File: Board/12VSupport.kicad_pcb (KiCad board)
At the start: 2 copper layers, 106.7 x 123.2 mm, 84 parts, among them J1 12V, J2 BATT, J3 BUCK_IN, J4 BUCK_OUT, J5 BOOST_IN, J6 BOOST_OUT, J7 TMP36GZ, J8 HEATER, J9 ICSP, K1 SLA-05VDC-SL-C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

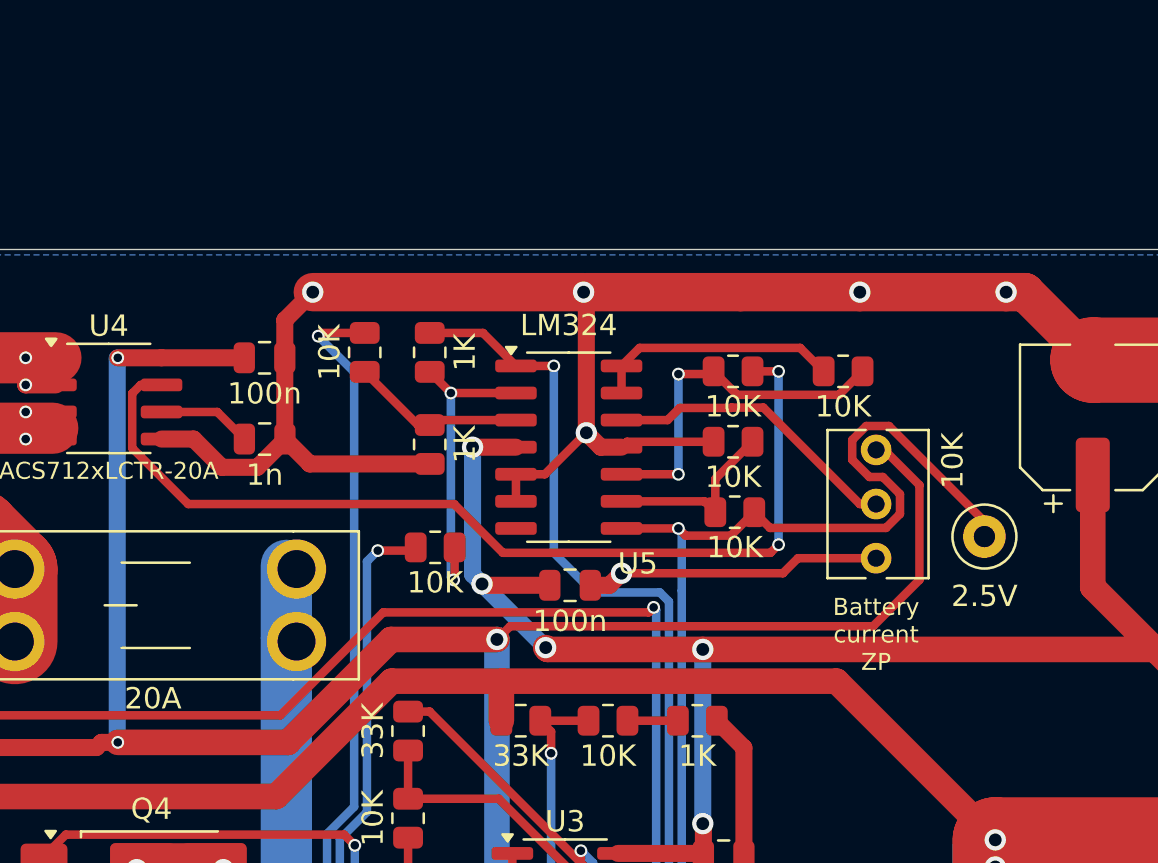
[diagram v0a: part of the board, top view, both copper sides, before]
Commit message: Schematic fixes
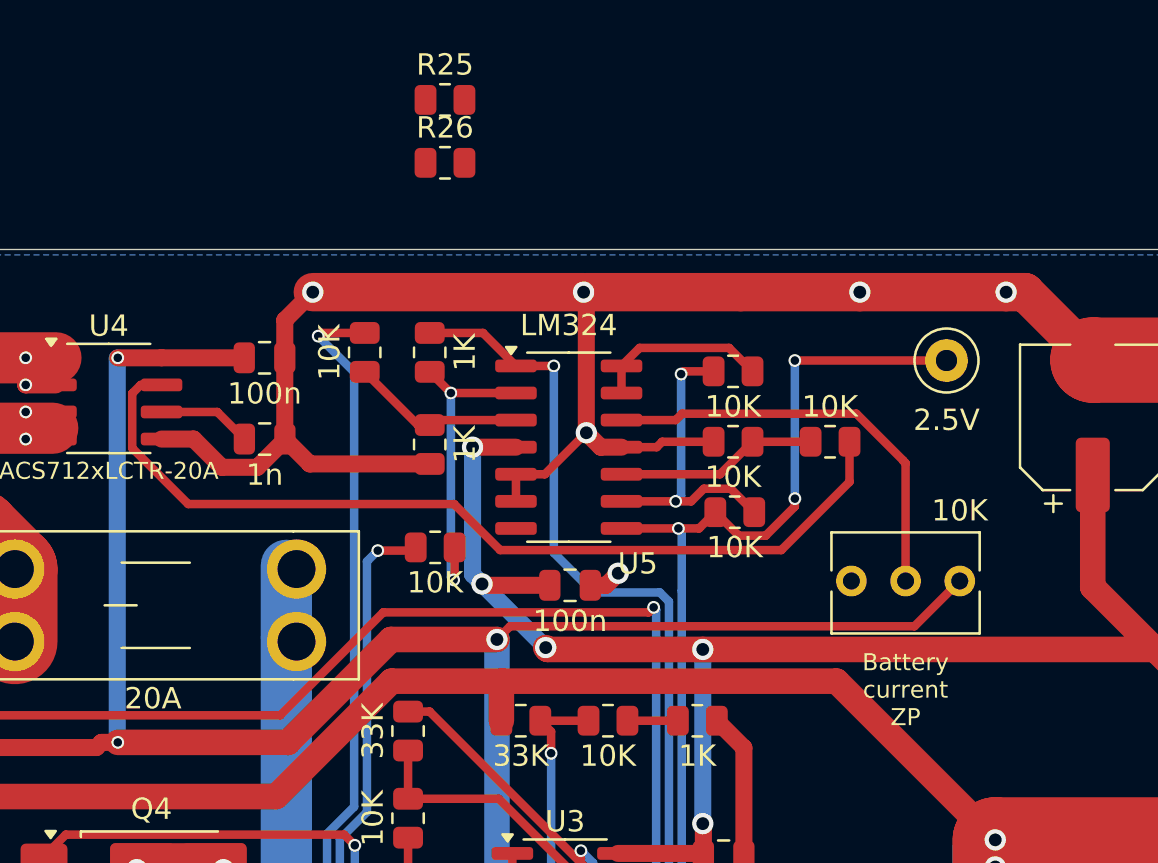
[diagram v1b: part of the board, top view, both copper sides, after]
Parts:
- added R25: 100K, Resistor_SMD:R_0805_2012Metric, F.Cu at (80.4, 34.9)
- added R26: 100K, Resistor_SMD:R_0805_2012Metric, F.Cu at (80.4, 37.8)
- moved TP1 8.44 mm to (103.9, 47.1)
- moved RV1 7.29 mm to (104.5, 57.5), turned to 0 degrees
- moved R22 3.36 mm to (98.4, 50.9), turned to 180 degrees
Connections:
- R19 pad 1: Net-(U5C--) -> CURR_SENSE
- R19 pad 2: CURR_SENSE -> Net-(U5C--)
- R20 pad 2: Net-(U5C--) -> Net-(U5C-+)
- R21 pad 1: Net-(U5C-+) -> Net-(U5C--)
- R21 pad 2: BAT_CURR -> /Sensors/VCC/2
- R22 pad 1: /Sensors/VCC/2 -> BAT_CURR
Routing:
- net GND: track 585.1 -> 572.8 mm
- net Net-(U5C-+): track 17.0 -> 9.50 mm, vias 2 -> 0
- net Net-(U5C--): track 8.63 -> 14.6 mm, vias 0 -> 2
- net Net-(U5D-+): track 14.1 -> 19.9 mm
- net VCC: track 345.4 -> 340.1 mm
- net CURR_SENSE: track 140.3 -> 135.7 mm, vias 2 -> 4
- net /Sensors/VCC/2: track 11.6 -> 7.62 mm
- net BAT_CURR: track 46.0 -> 42.9 mm, vias 2 -> 0

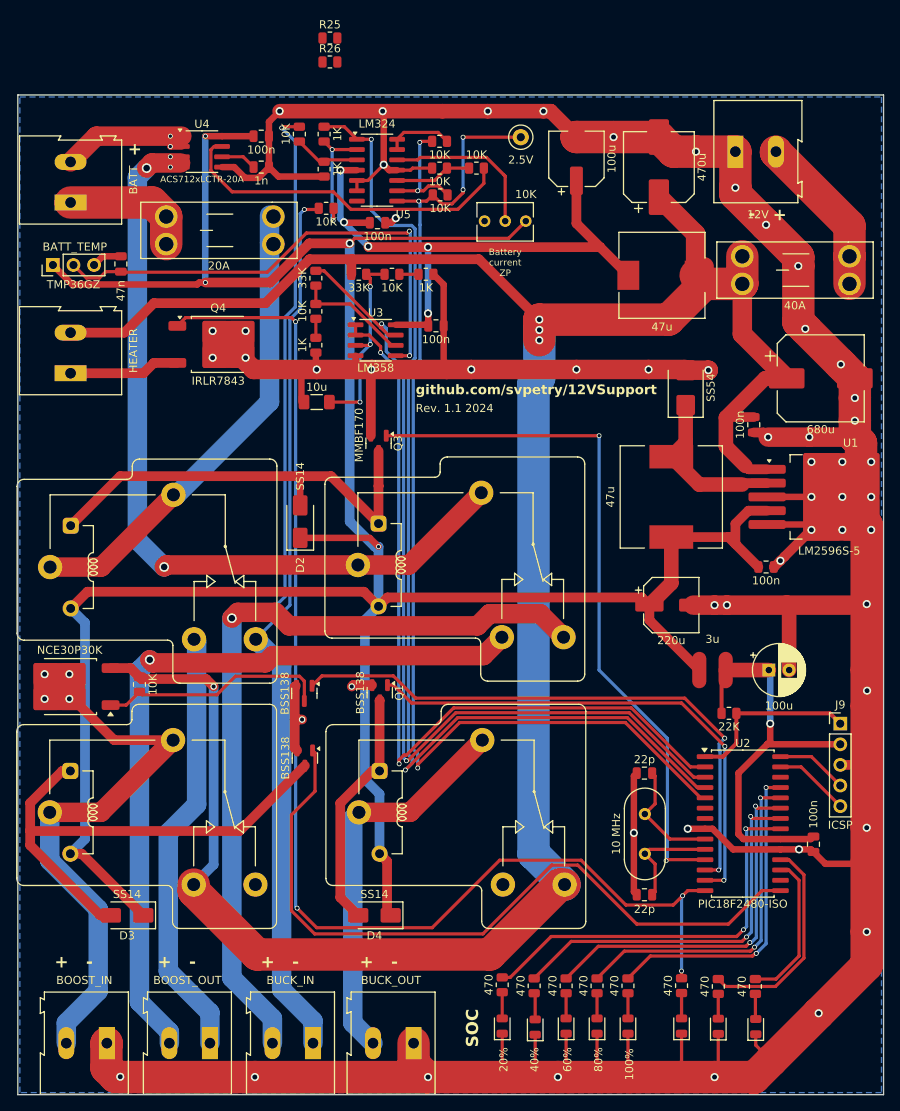
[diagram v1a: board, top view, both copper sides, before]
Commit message: Fixes battery voltage sensing.
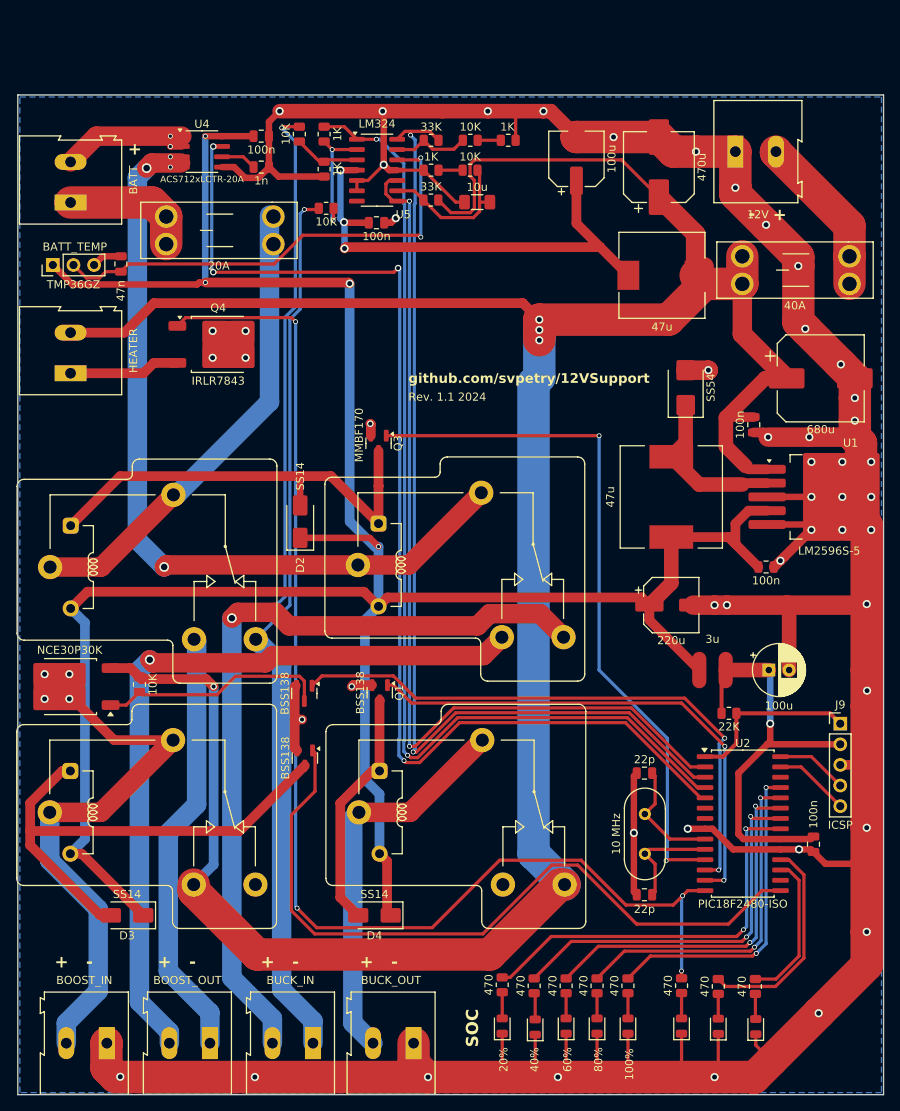
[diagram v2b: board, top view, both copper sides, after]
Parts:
- removed C10: 100n, Capacitor_SMD:C_0805_2012Metric
- removed R19, R20, R21, R22: 10K, Resistor_SMD:R_0805_2012Metric
- removed R25, R26: 100K, Resistor_SMD:R_0805_2012Metric
- removed RV1: 10K, Potentiometer_THT:Potentiometer_Bourns_3266Y_Vertical
- removed TP1: 2.5V, TestPoint:TestPoint_Loop_D1.80mm_Drill1.0mm_Beaded
- removed U3: LM358, Package_SO:SOIC-8_3.9x4.9mm_P1.27mm
- moved R4 34.6 mm to (102.3, 47.5), turned to 0 degrees
- moved C6 31.6 mm to (98.5, 55.1)
- moved R3 28.4 mm to (97.7, 47.5), turned to 0 degrees
- moved R2 22.1 mm to (92.8, 47.5), turned to 180 degrees
- moved R6 16.0 mm to (97.6, 51.2), turned to 180 degrees
- moved C8 14.7 mm to (86.1, 57.7)
- moved R7 12.8 mm to (92.8, 51.2), turned to 180 degrees
- moved R5 12.8 mm to (92.8, 54.9), turned to 180 degrees
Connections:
- C6 pad 1: Net-(U3A-+) -> Net-(U5C--)
- R2 pad 2: Net-(U3B--) -> Net-(U5D--)
- R3 pad 1: Net-(U3B--) -> Net-(U5D--)
- R5 pad 2: Net-(U3A-+) -> Net-(U5C--)
- R6 pad 1: Net-(U3A-+) -> Net-(U5C--)
- U4 pad 7: BAT_CURR -> CURR_SENSE
- U5 pad 10: Net-(U5C-+) -> 12V_SENSE
- U5 pad 12: Net-(U5D-+) -> Net-(J7-Pin_2)
- U5 pad 13: /Sensors/VCC/2 -> Net-(U5D--)
- U5 pad 14: /Sensors/VCC/2 -> TEMP_SENSE
- U5 pad 8: CURR_SENSE -> 12V_SENSE
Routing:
- net GND: track 572.8 -> 497.2 mm, vias 54 -> 50
- net BAT_CURR: track 42.9 -> 0.00 mm
- net +12V: track 314.9 -> 344.9 mm
- net VCC: track 340.1 -> 310.3 mm
- net Net-(U3A-+): track 24.2 -> 0.00 mm, vias 3 -> 0
- net Net-(U5D-+): track 19.9 -> 0.00 mm
- net Net-(U3B--): track 14.2 -> 0.00 mm
- net 12V_SENSE: track 101.1 -> 114.6 mm
- net TEMP_SENSE: track 111.3 -> 124.1 mm
- net /Sensors/V+_OP: track 72.7 -> 61.0 mm, vias 5 -> 3
- net Net-(U5C-+): track 9.50 -> 0.00 mm
- net Net-(U5D--): track 0.00 -> 9.49 mm
- net CURR_SENSE: track 135.7 -> 143.9 mm
- net /Sensors/VCC/2: track 7.62 -> 0.00 mm
- net BAT_SENSE: track 132.3 -> 127.3 mm
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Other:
- board text removed: "Battery current ZP"

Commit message: Schematic/layout improvements.
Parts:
- added D14: SS14, Diode_SMD:D_SMA, F.Cu at (120.0, 74.3)
- added D15: POWER, LED_SMD:LED_0805_2012Metric, F.Cu at (142.3, 102.4)
- added D5: SS14, Diode_SMD:D_SMA, F.Cu at (130.8, 72.4)
- added R19: 680, Resistor_SMD:R_0805_2012Metric, F.Cu at (137.1, 102.4)
- moved D1 4.97 mm to (120.0, 80.6), turned to 180 degrees
- moved C4 1.08 mm to (133.3, 99.3)
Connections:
- C2 pad 1: +12V -> Net-(D14-K)
- C5 pad 1: +12V -> Net-(D14-K)
- U1 pad 1: +12V -> Net-(D14-K)
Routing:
- net /BUCK_OUT+: track 48.7 -> 123.2 mm, vias 0 -> 1
- net Net-(D14-K): track 0.00 -> 36.0 mm
- net +12V: track 344.9 -> 313.4 mm
- net /Sensors/V+_OP: track 61.0 -> 50.8 mm, vias 3 -> 0
- net Net-(U5A--): track 14.8 -> 21.4 mm, vias 2 -> 0
- net VCC: track 310.3 -> 314.3 mm
- net Net-(D15-A): track 0.00 -> 3.30 mm
- net GND: track 497.2 -> 499.0 mm, vias 50 -> 51
- net Net-(J7-Pin_2): track 58.6 -> 60.3 mm
- net BUCK+: track 167.0 -> 165.6 mm
- net Net-(D1-K): track 20.4 -> 19.3 mm
- net CURR_SENSE: track 143.9 -> 143.0 mm
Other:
- outline, holes or cut-outs redrawn
- board text added: "CHG"
- board text added: "DCHG"
- board text added: "HTR"

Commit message: 1.1 improvements
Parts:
- added REF**: MountingHole_3.2mm_M3_Pad_Via, MountingHole:MountingHole_3.2mm_M3_Pad_Via, F.Cu at (143.5, 47.0)
- added REF**: MountingHole_3.2mm_M3_Pad_Via, MountingHole:MountingHole_3.2mm_M3_Pad_Via, F.Cu at (143.5, 160.0)
- added REF**: MountingHole_3.2mm_M3_Pad_Via, MountingHole:MountingHole_3.2mm_M3_Pad_Via, F.Cu at (47.0, 144.5)
- added REF**: MountingHole_3.2mm_M3_Pad_Via, MountingHole:MountingHole_3.2mm_M3_Pad_Via, F.Cu at (47.0, 83.8)
- U2: value PIC18F2480-ISO -> PIC18F2480
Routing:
- net GND: track 499.0 -> 508.2 mm, vias 51 -> 52
- net 12V_SENSE: track 114.6 -> 108.0 mm
- net BAT_SENSE: track 127.3 -> 121.0 mm
- net CURR_SENSE: track 143.0 -> 136.7 mm
- net TEMP_SENSE: track 123.6 -> 117.9 mm
- net Net-(K2-Pad11A): track 98.3 -> 103.4 mm, vias 4 -> 6
- net REL_BOOST_IN: track 90.8 -> 86.7 mm
- net Net-(D2-A): track 55.4 -> 59.2 mm
- net REL_CHARGE: track 87.0 -> 89.5 mm
- net EN_BOOST_IN: track 72.9 -> 71.9 mm
- net BUCK+: track 165.6 -> 166.3 mm
- net +12V: track 313.4 -> 314.0 mm
- net REL_HEATER: track 155.5 -> 155.0 mm

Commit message: Minor improvements
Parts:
- added REF**: OSHW-Logo_11.4x12mm_SilkScreen, Symbol:OSHW-Logo_11.4x12mm_SilkScreen, F.Cu at (87.9, 67.8)
- added REF**: ESD-Logo_13.2x12mm_SilkScreen, Symbol:ESD-Logo_13.2x12mm_SilkScreen, F.Cu at (102.1, 67.3)
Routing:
- net /BOOST_IN+: track 65.9 -> 68.1 mm
- net Net-(J6-Pin_2): track 94.2 -> 93.4 mm

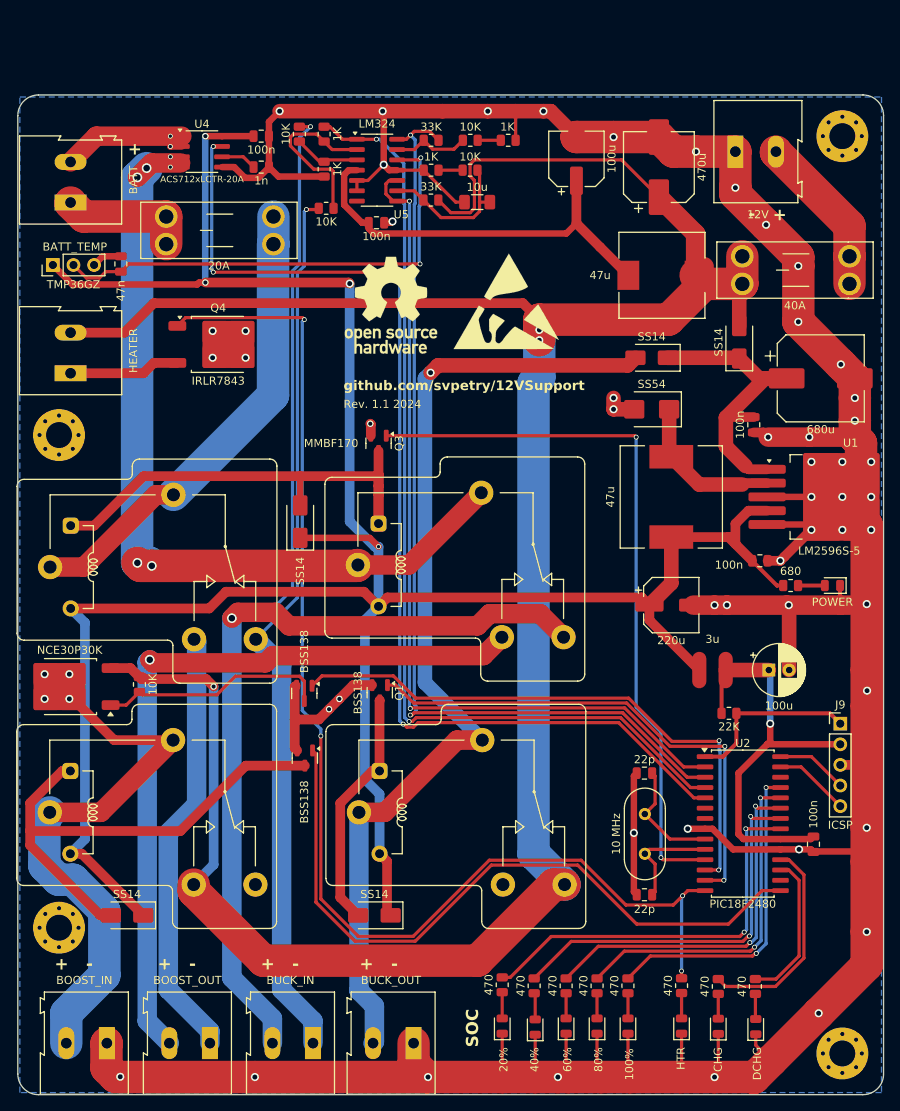
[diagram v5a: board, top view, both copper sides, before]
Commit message: Larger screw terminals.
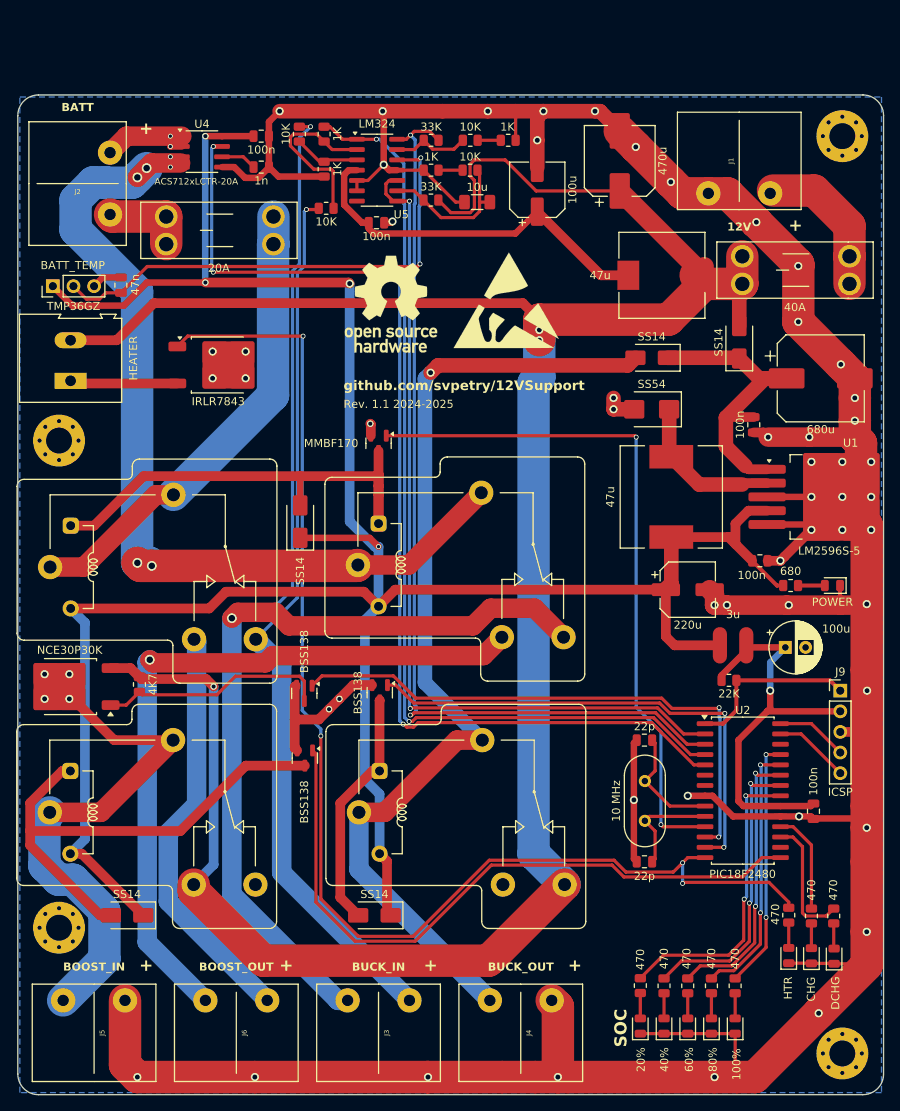
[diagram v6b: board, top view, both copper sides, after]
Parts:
- J1, J2, J3, J4, J5, J6: footprint TerminalBlock:TerminalBlock_Altech_AK300-2_P5.00mm -> spetry:KF7.62_2P
- R24: value 10K -> 4K7
- moved R12 17.0 mm to (118.6, 151.7)
- moved D9 17.0 mm to (118.6, 156.6)
- moved R13 16.0 mm to (121.5, 151.7)
- moved D10 15.9 mm to (121.5, 156.6)
- moved R11 15.8 mm to (136.9, 143.0)
- moved D8 15.8 mm to (136.9, 148.0)
- moved D11 15.0 mm to (124.5, 156.6)
- moved R14 15.0 mm to (124.5, 151.7)
- moved D7 14.4 mm to (139.7, 148.0)
- moved R10 14.4 mm to (139.7, 143.1)
- moved D12 14.1 mm to (127.4, 156.6)
- moved R15 14.1 mm to (127.4, 151.7)
- moved J4 13.3 mm to (103.9, 157.5)
- moved D13 13.2 mm to (130.3, 156.6)
- moved R16 13.2 mm to (130.3, 151.7)
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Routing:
- net GND: track 508.2 -> 493.5 mm, vias 52 -> 53
- net Net-(U2-RX/DT/RC7): track 26.3 -> 12.6 mm
- net Net-(U2-RB0/INT0/AN10): track 49.3 -> 36.9 mm
- net Net-(U2-RB1/INT1/AN8): track 47.4 -> 35.9 mm
- net Net-(U2-RB2/AN8/INT2/CANTX): track 44.9 -> 34.3 mm
- net Net-(U2-RB3/CANRX): track 42.3 -> 32.4 mm
- net Net-(K2-Pad11A): track 103.4 -> 112.5 mm
- net Net-(U2-RB4/KBI0/AN9): track 39.8 -> 30.9 mm
- net /BAT-: track 16.0 -> 10.4 mm
- net /BAT+: track 17.7 -> 12.4 mm
- net /BOOST_IN+: track 68.1 -> 63.0 mm
- net REL_CHARGE: track 89.5 -> 85.4 mm
- net /Sensors/V+_OP: track 50.8 -> 46.8 mm
- net Net-(J6-Pin_2): track 93.4 -> 89.9 mm
- net REL_HEATER: track 155.0 -> 158.4 mm
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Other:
- board text added: "Rev. 1.1 2024-2025"
- board text removed: "+ -"
- board text removed: "Rev. 1.1 2024"
